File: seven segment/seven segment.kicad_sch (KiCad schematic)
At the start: 6 parts, among them U2 CC56-12EWA, U8 TM1637

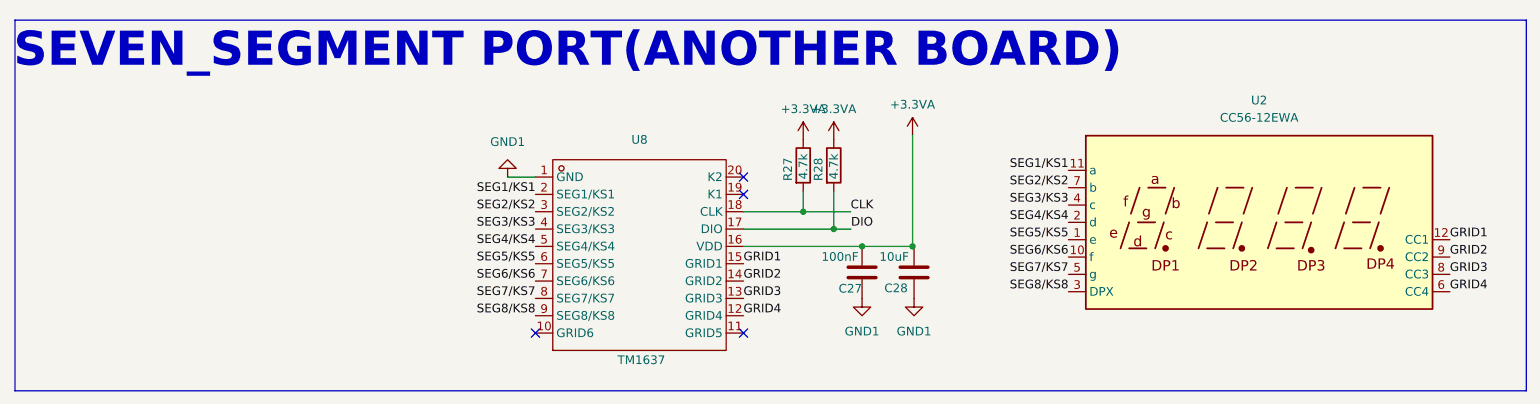
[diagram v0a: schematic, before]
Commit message: -
update seven segment
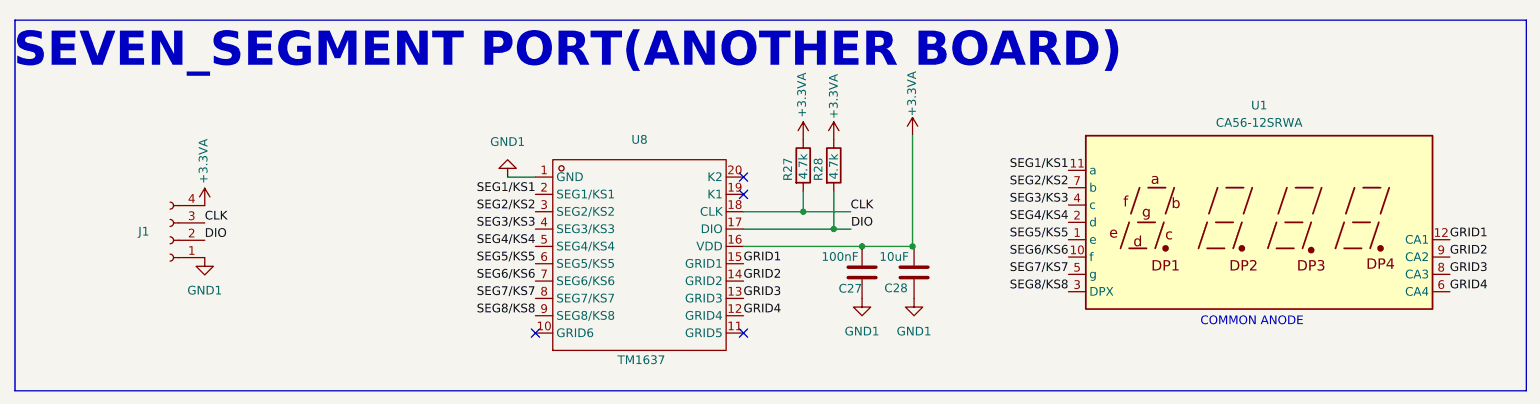
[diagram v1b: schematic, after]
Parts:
- removed U2: CC56-12EWA, Display_7Segment:CA56-12EWA, symbol Display_Character:CC56-12EWA
- added J1: Conn_01x04_Socket, symbol Connector:Conn_01x04_Socket
- added U1: CA56-12SRWA, Display_7Segment:CA56-12SRWA, symbol Display_Character:CA56-12SRWA
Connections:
- net +3.3VA: now also J1.4 (Pin_4)
- net CLK: now also J1.3 (Pin_3)
- net DIO: now also J1.2 (Pin_2)
- net GND1: now also J1.1 (Pin_1)
- net GRID1: now also U1.12 (CA1)
- net GRID2: now also U1.9 (CA2)
- net GRID3: now also U1.8 (CA3)
- net GRID4: now also U1.6 (CA4)
- net SEG1/KS1: now also U1.11 (a)
- net SEG2/KS2: now also U1.7 (b)
- net SEG3/KS3: now also U1.4 (c)
- net SEG4/KS4: now also U1.2 (d)
- net SEG5/KS5: now also U1.1 (e)
- net SEG6/KS6: now also U1.10 (f)
- net SEG7/KS7: now also U1.5 (g)
- net SEG8/KS8: now also U1.3 (DPX)
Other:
- note added: "COMMON ANODE"

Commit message: -
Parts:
- J1: footprint (none) -> Connector_JST:JST_EH_B4B-EH-A_1x04_P2.50mm_Vertical
- U2: renamed from U8; footprint InnovKits:SOP-20_L12.8-W7.5-P1.27-LS10.4-BL -> Footprint:SOP-20_L12.8-W7.5-P1.27-LS10.4-BL
- renumbered C27 to C1, C28 to C2, R27 to R1, R28 to R2
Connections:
- net +3.3VA: now also J1.1 (Pin_1); no longer J1.4 (Pin_4)
- net CLK: now also J1.2 (Pin_2); no longer J1.3 (Pin_3)
- net DIO: now also J1.3 (Pin_3); no longer J1.2 (Pin_2)
- net GND1: now also J1.4 (Pin_4); no longer J1.1 (Pin_1)
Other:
- moved on the sheet: J1
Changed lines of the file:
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@@
 		(on_board yes)
 		(dnp no)
-		(property "Reference" "C28"
+		(property "Reference" "C2"
 			(at 167.2044 64.46 0)
 			(effects
@@
 			(project "seven segment"
 				(path "/f35e8fbd-20e2-4e8b-a22f-f96068be6e33"
-					(reference "C28")
+					(reference "C2")
 					(unit 1)
 				)
@@
 		(on_board yes)
 		(dnp no)
-		(property "Reference" "U8"
+		(property "Reference" "U2"
 			(at 131.3297 42.7062 0)
 			(effects
@@
 			)
 		)
-		(property "Footprint" "InnovKits:SOP-20_L12.8-W7.5-P1.27-LS10.4-BL"
+		(property "Footprint" "Footprint:SOP-20_L12.8-W7.5-P1.27-LS10.4-BL"
 			(at 131.3297 59.6044 0)
 			(effects
@@
 			(project "seven segment"
 				(path "/f35e8fbd-20e2-4e8b-a22f-f96068be6e33"
-					(reference "U8")
+					(reference "U2")
 					(unit 1)
 				)
@@
 	(symbol
 		(lib_id "Connector:Conn_01x04_Socket")
-		(at 62.5565 57.4382 180)
+		(at 62.5565 54.8982 0)
+		(mirror y)
 		(unit 1)
 		(exclude_from_sim no)
@@
 		(dnp no)
 		(property "Reference" "J1"
-			(at 58.7092 56.156 0)
+			(at 58.7092 56.1804 0)
 			(effects
 				(font
@@
 		)
 		(property "Value" "Conn_01x04_Socket"
-			(at 63.1915 49.53 0)
-			(effects
-				(font
-					(size 1.27 1.27)
-				)
-				(hide yes)
-			)
-		)
-		(property "Footprint" ""
-			(at 62.5565 57.4382 0)
+			(at 63.1915 62.8064 0)
+			(effects
+				(font
+					(size 1.27 1.27)
+				)
+				(hide yes)
+			)
+		)
+		(property "Footprint" "Connector_JST:JST_EH_B4B-EH-A_1x04_P2.50mm_Vertical"
+			(at 62.5565 54.8982 0)
 			(effects
 				(font
@@
 		)
 		(property "Datasheet" "~"
-			(at 62.5565 57.4382 0)
+			(at 62.5565 54.8982 0)
 			(effects
 				(font
@@
 		)
 		(property "Description" "Generic connector, single row, 01x04, script generated"
-			(at 62.5565 57.4382 0)
+			(at 62.5565 54.8982 0)
 			(effects
 				(font
@@
 		(on_board yes)
 		(dnp no)
-		(property "Reference" "R28"
+		(property "Reference" "R2"
 			(at 157.5487 48.7648 90)
 			(effects
@@
 			(project "seven segment"
 				(path "/f35e8fbd-20e2-4e8b-a22f-f96068be6e33"
-					(reference "R28")
+					(reference "R2")
 					(unit 1)
 				)
@@
 		(on_board yes)
 		(dnp no)
-		(property "Reference" "C27"
+		(property "Reference" "C1"
 			(at 163.9388 64.5194 0)
 			(effects
@@
 			(project "seven segment"
 				(path "/f35e8fbd-20e2-4e8b-a22f-f96068be6e33"
-					(reference "C27")
+					(reference "C1")
 					(unit 1)
 				)
@@
 		(on_board yes)
 		(dnp no)
-		(property "Reference" "R27"
+		(property "Reference" "R1"
 			(at 153.0759 48.7648 90)
 			(effects
@@
 			(project "seven segment"
 				(path "/f35e8fbd-20e2-4e8b-a22f-f96068be6e33"
-					(reference "R27")
-					(unit 1)
-				)
+					(reference "R1")
+					(unit 1)
+				)
